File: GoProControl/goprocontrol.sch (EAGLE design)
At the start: 19 parts, among them Q1 IRLML6344

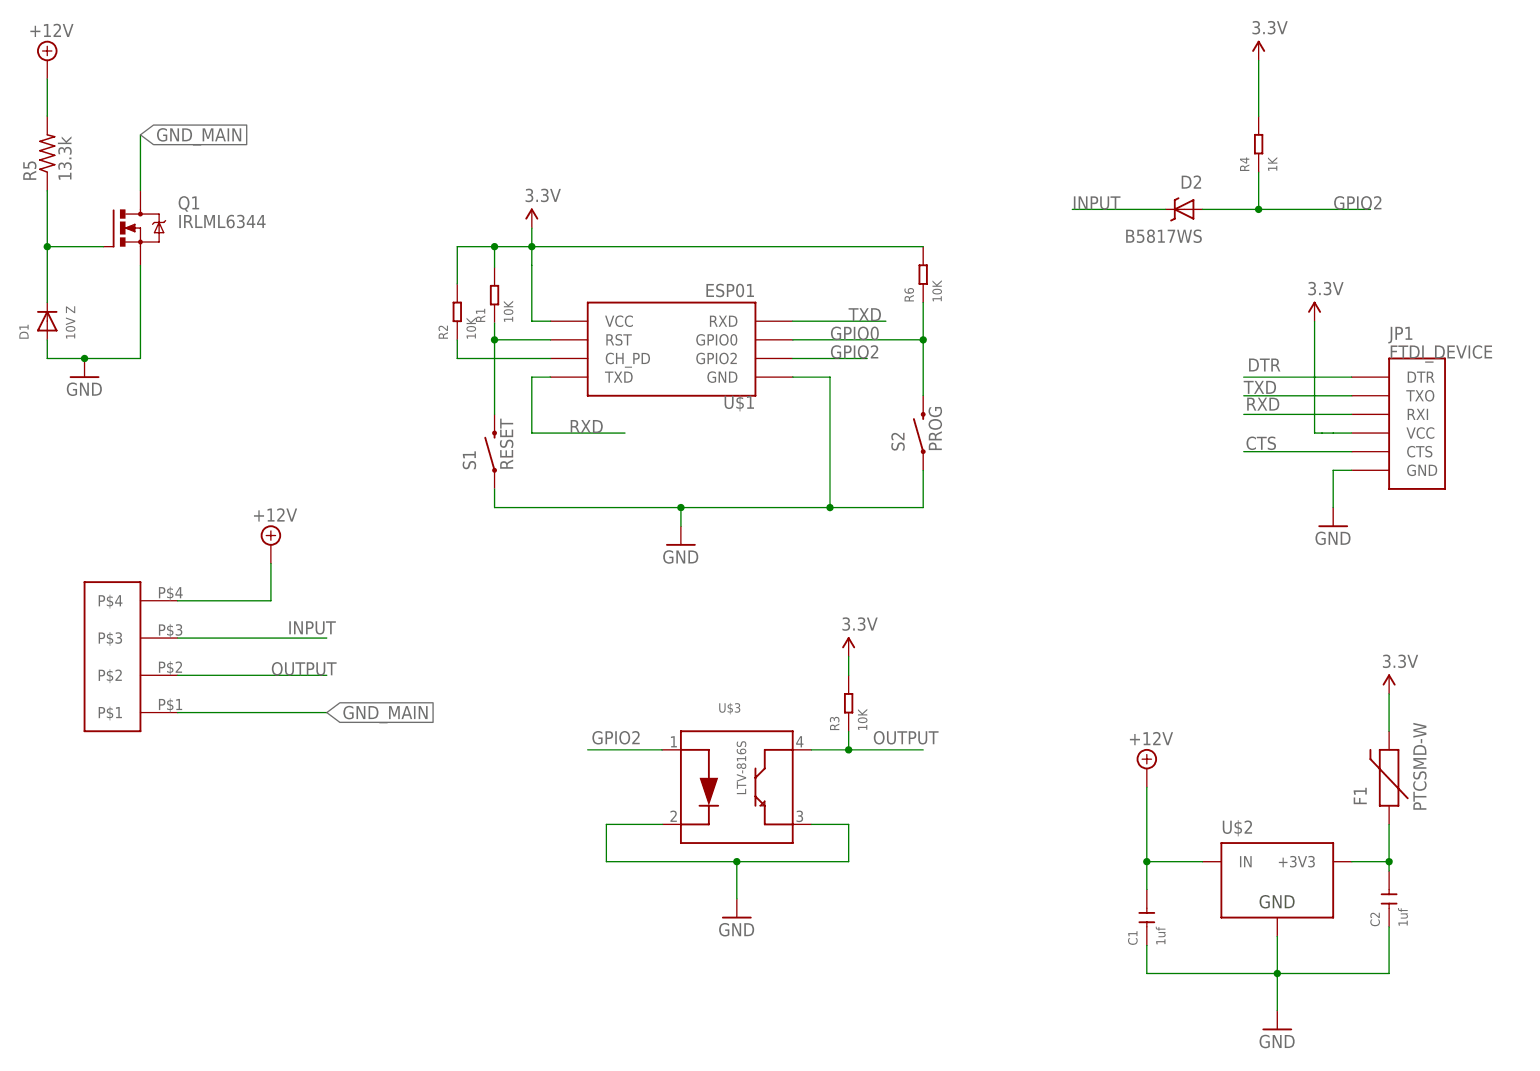
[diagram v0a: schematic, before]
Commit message: Update PCB to v0.5
- Switch to using more common 5V FTDI (VCC & signal)
- Use Schottky diodes to protect reverse polarity and
  to make sure we don't send 12V onto the FTDI VCC line
- Add 1uF cap to VCC on ESP8266 to stabilize things

Still would be a good idea to protect against the FTDI
cable being inserted backwards and putting 5V onto RXD
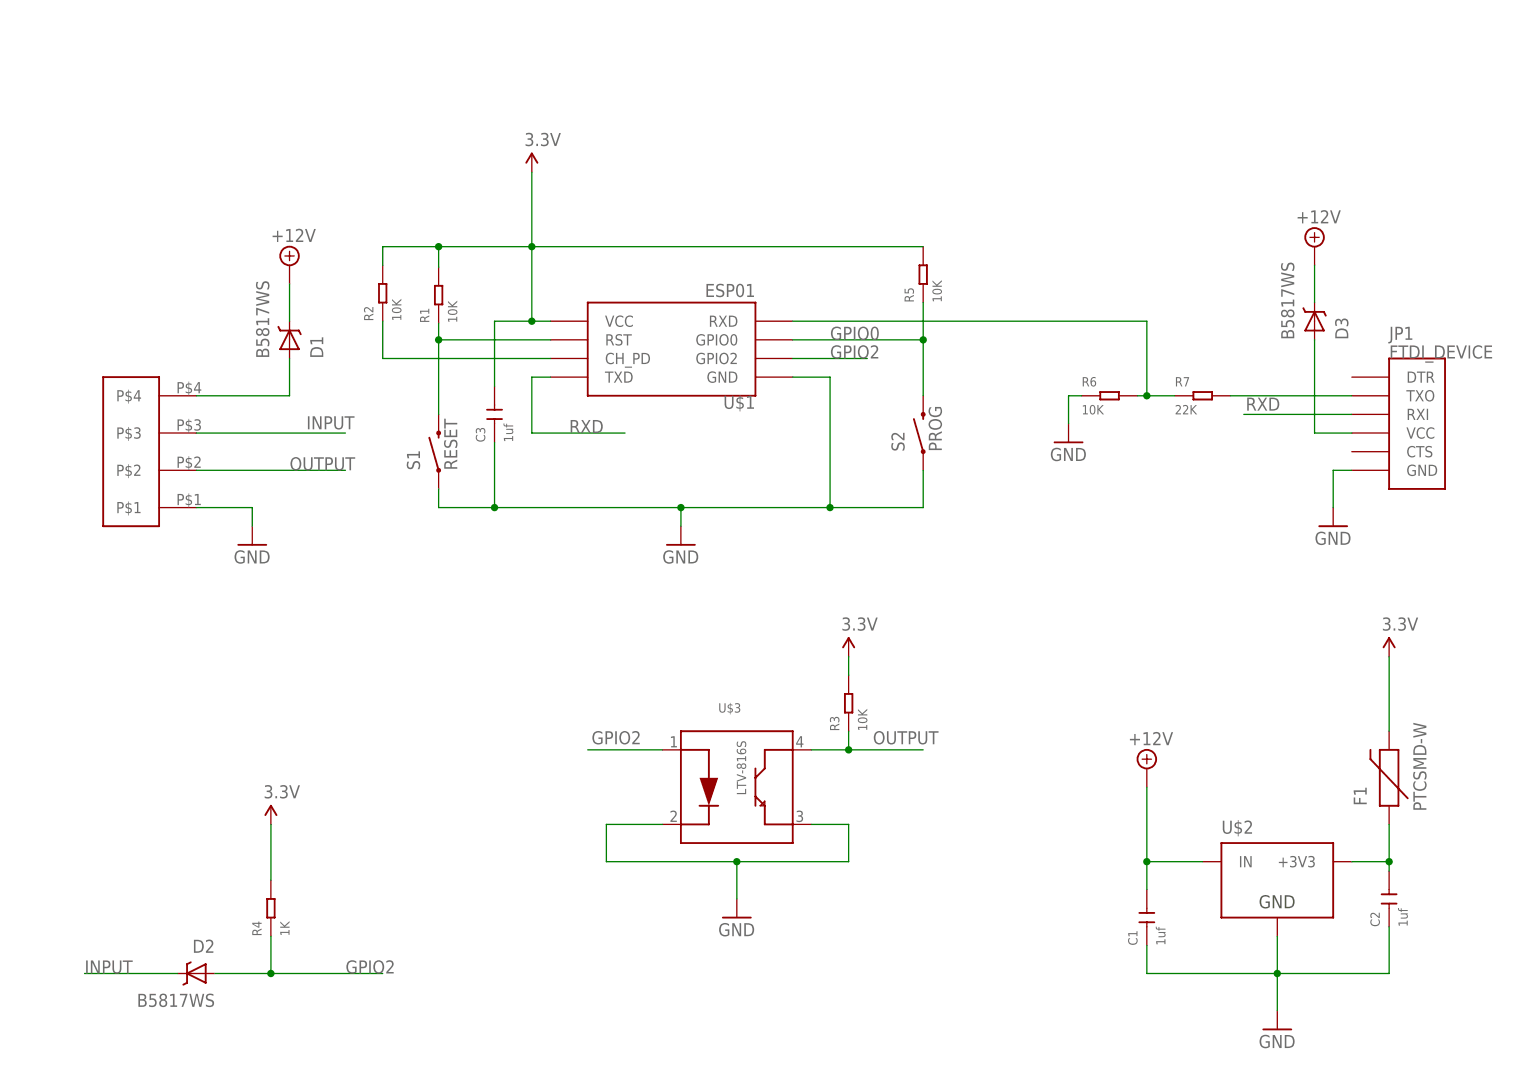
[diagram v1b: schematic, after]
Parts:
- removed Q1: IRLML6344, synfinatic:IRLML6344
- added C3: 1uf, Seeed-OPL-Capacitor:CERAMIC-1UF-25V-10%-X7R(0805)
- added D3: B5817WS, synfinatic:SCHOTTKY-DIODE
- added R7: 22K, Seeed-OPL-Resistor:SMD-RES-22K-5%-1/8W(0805)
- D1: value 10V Z -> B5817WS; device adafruit:DIODESOD-123 -> synfinatic:SCHOTTKY-DIODE
- R5: value 13.3k -> 10K; device resistor:R-US_M0805 -> Seeed-OPL-Resistor:SMD-RES-10K-1%-1/8W(0805)
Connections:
- removed net CTS: JP1.CTS
- removed net DTR: JP1.DTR
- removed net GND_MAIN: Q1.D, U$4.P$1
- removed net N$17: D1.C, Q1.G, R5.1
- new net N$4: D3.A, JP1.VCC
- new net N$6: D1.A, U$4.P$4
- new net N$8: JP1.TXO, R7.2
- net +12V: now also D1.C, D3.C; no longer R5.2, U$4.P$4
- net 3.3V: now also C3.2, R5.2; no longer JP1.VCC, R6.2
- net GND: now also C3.1, R6.1, U$4.P$1; no longer D1.A, Q1.S
- net GPIO0: now also R5.1; no longer R6.1
- net TXD: now also R6.2, R7.1; no longer JP1.TXO
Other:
- moved on the sheet: D2, R1, R2, R4, R6, S1

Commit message: Update PCB to v0.6
- Replace LDO with a switching module
- Update readme file
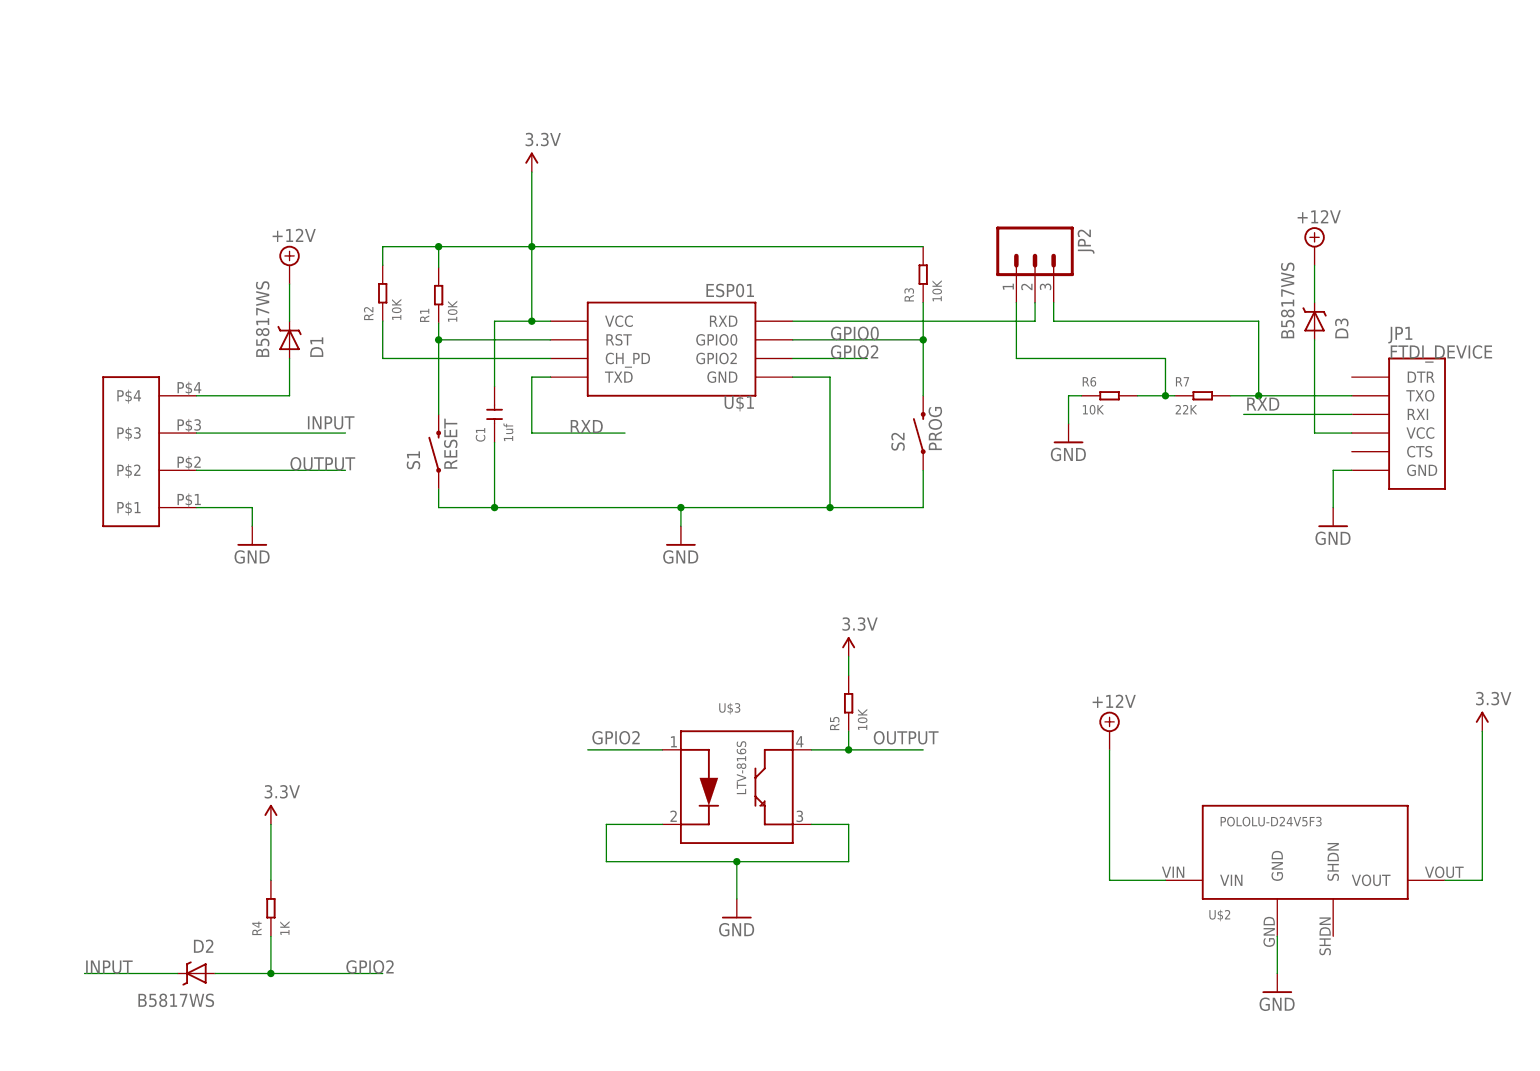
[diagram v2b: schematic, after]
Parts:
- removed C2, C3: 1uf, Seeed-OPL-Capacitor:CERAMIC-1UF-25V-10%-X7R(0805)
- removed F1: PTCSMD-W, SparkFun-PowerIC:PTCSMD-W
- added JP2: (no value), SparkFun-Connectors:M03PTH
- U$2: value MCP1825SOT-223-3 -> POLOLU-D24V5F3; device synfinatic:MCP1825SOT-223-3 -> synfinatic:POLOLU-D24V5FD24V5F
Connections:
- removed net 3.3-UNPRO: C2.2, F1.1, U$2.+3V3
- removed net N$8: JP1.TXO, R7.2
- new net 3.3V-TX: JP1.TXO, JP2.3, R7.2
- new net 5V-TX: JP2.1, R6.2, R7.1
- net +12V: now also U$2.VIN; no longer C1.2, U$2.IN
- net 3.3V: now also C1.2, U$2.VOUT; no longer C3.2, F1.2
- net GND: no longer C2.1, C3.1
- net GPIO0: now also R3.1; no longer R5.1
- net OUTPUT: now also R5.1; no longer R3.1
- net TXD: now also JP2.2; no longer R6.2, R7.1
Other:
- moved on the sheet: C1, R3, R5

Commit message: Update board to v0.7
- Fixes FTDI RX/TX reversal
- Fixes GPIO2 pullup
- Rotated termblock
- Still needs to fix term block part to match
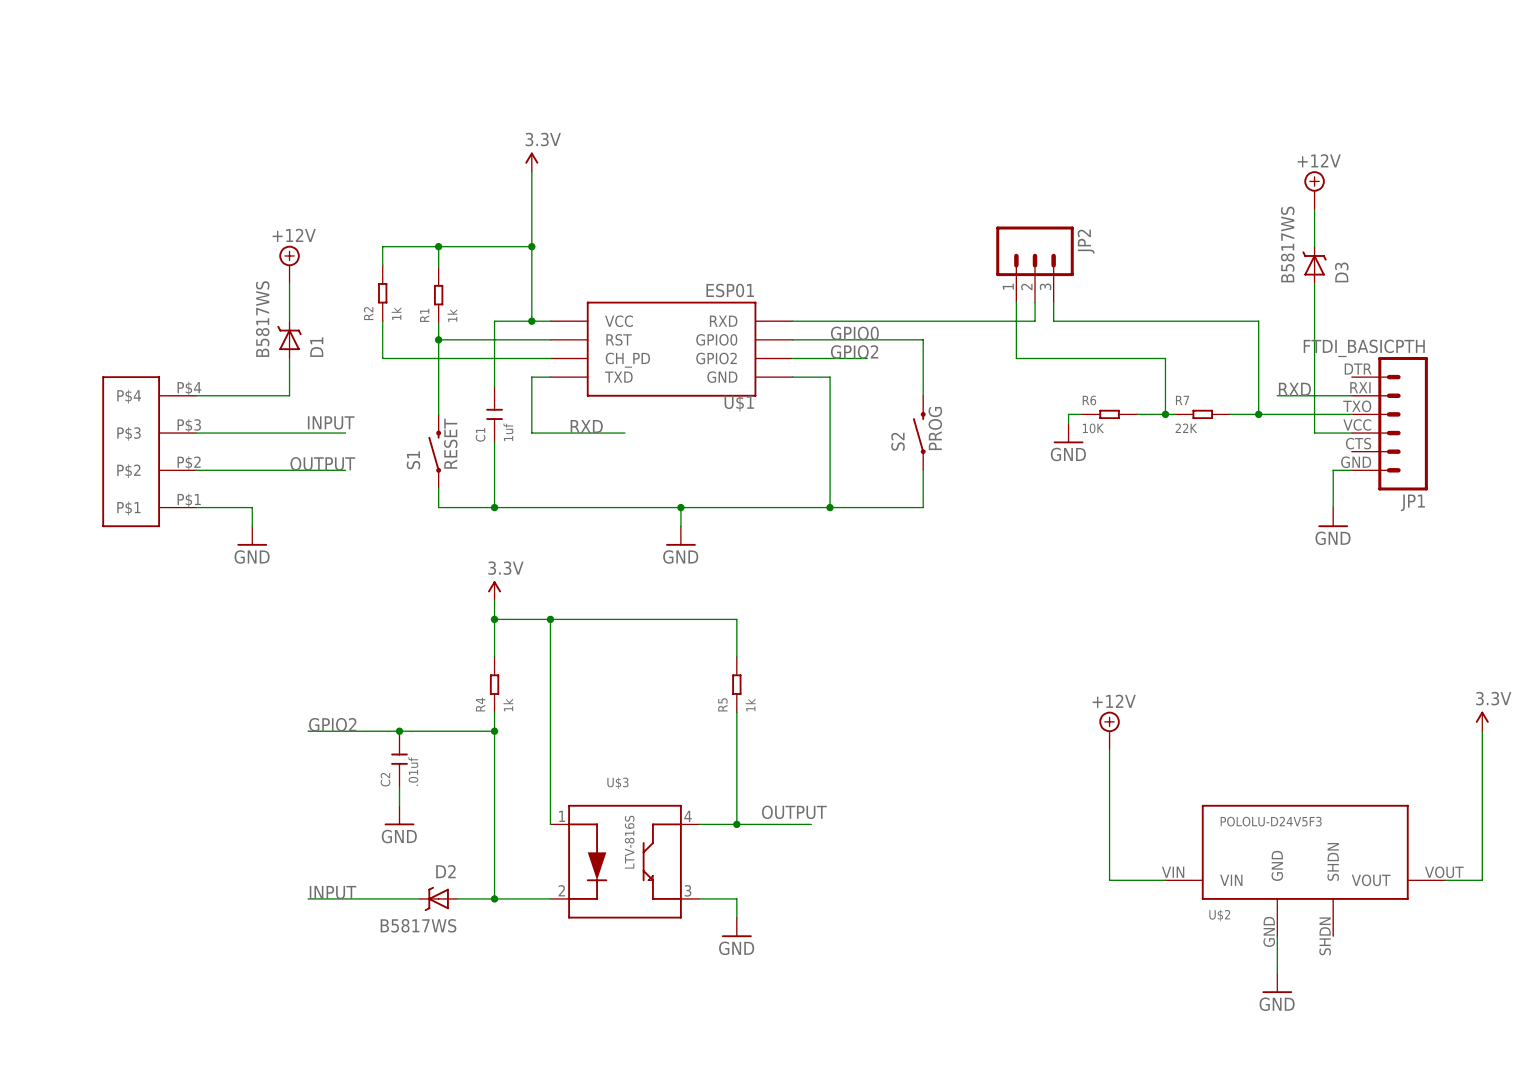
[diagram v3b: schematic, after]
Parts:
- removed R3: 10K, Seeed-OPL-Resistor:SMD-RES-10K-1%-1/8W(0805)
- added C2: .01uf, Seeed-OPL-Capacitor:CERAMIC-1UF-25V-10%-X7R(0805)
- JP1: value FTDI_DEVICE -> FTDI_BASICPTH; device SparkFun-Connectors:FTDI_DEVICE -> SparkFun-Connectors:FTDI_BASICPTH
- R1, R2, R5: value 10K -> 1k
- R4: value 1K -> 1k; device Seeed-OPL-Resistor:SMD-RES-1K-5%-1/8W(0805) -> Seeed-OPL-Resistor:SMD-RES-10K-1%-1/8W(0805)
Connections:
- net 3.3V: now also U$3.ANODE; no longer R3.2
- net 3.3V-TX: now also JP1.3; no longer JP1.TXO
- net GND: now also C2.1, JP1.6; no longer JP1.GND, U$3.CATHODE
- net GPIO0: no longer R3.1
- net GPIO2: now also C2.2, U$3.CATHODE; no longer U$3.ANODE
- net N$4: now also JP1.4; no longer JP1.VCC
- net RXD: now also JP1.2; no longer JP1.RXI
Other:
- moved on the sheet: D2, D3, R4, R5, R6, R7, U$3
